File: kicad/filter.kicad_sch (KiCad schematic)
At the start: 31 parts, among them J4 Conn_01x05, U4 NE5532, U5 NE5532, U6 NE5532, U7 NE5532

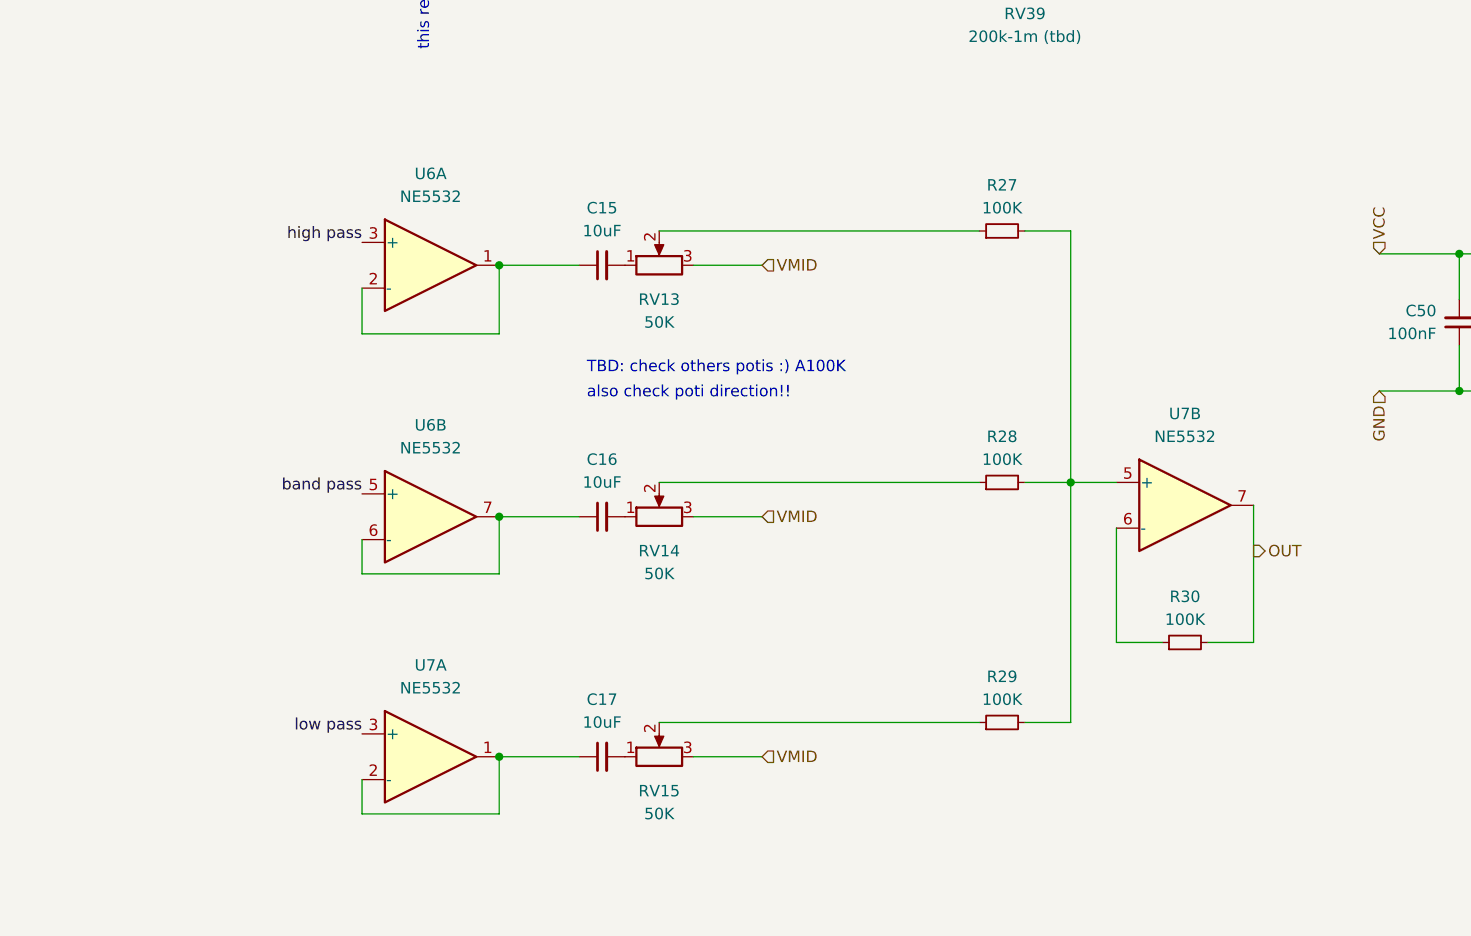
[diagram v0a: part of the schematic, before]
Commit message: fix mixers in filter and compressor, update pcb
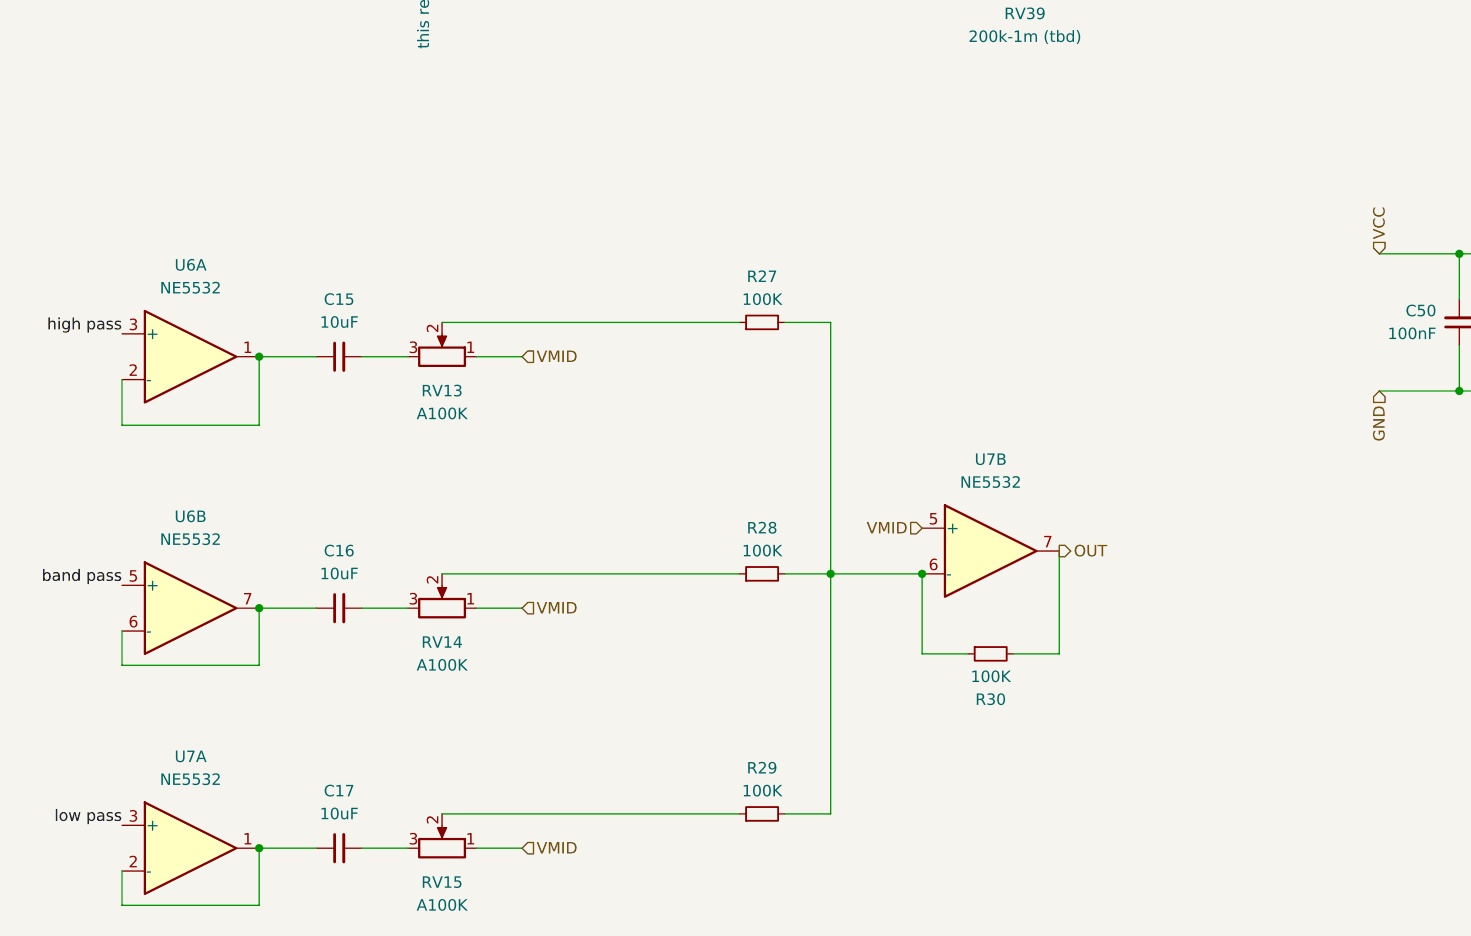
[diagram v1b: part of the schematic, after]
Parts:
- RV13, RV14, RV15: value 50K -> A100K
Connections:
- net VMID: now also RV13.1, RV14.1, RV15.1, U7.5 (+); no longer RV13.3, RV14.3, RV15.3
- net at C16.2: now also RV14.3; no longer RV14.1
- net at C15.2: now also RV13.3; no longer RV13.1
- net at C17.2: now also RV15.3; no longer RV15.1
- net at R27.2, R28.2, R29.2: now also R30.1, U7.6 (-); no longer U7.5 (+)
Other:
- note removed: "TBD: check others potis :) A100K"
- note removed: "also check poti direction!!"
- moved on the sheet: C15, C16, C17, R27, R28, R29, R30, RV13, RV14, RV15, U6A, U6B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

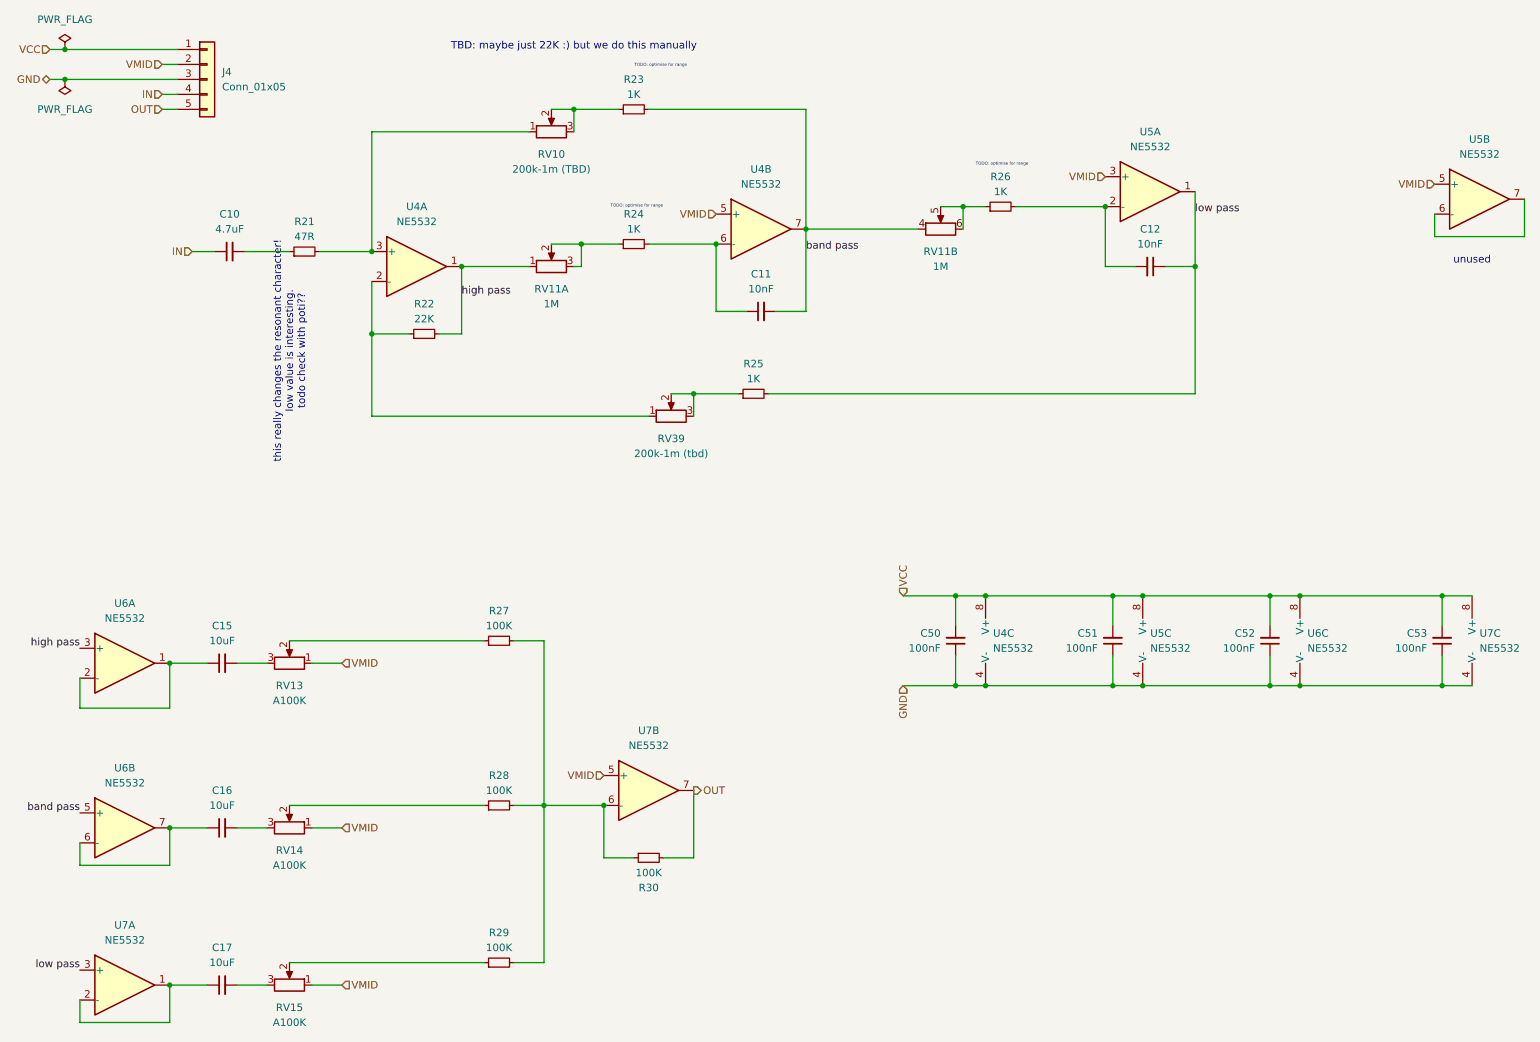
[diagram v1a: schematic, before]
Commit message: mark components as DNP, add LCSC part numbers
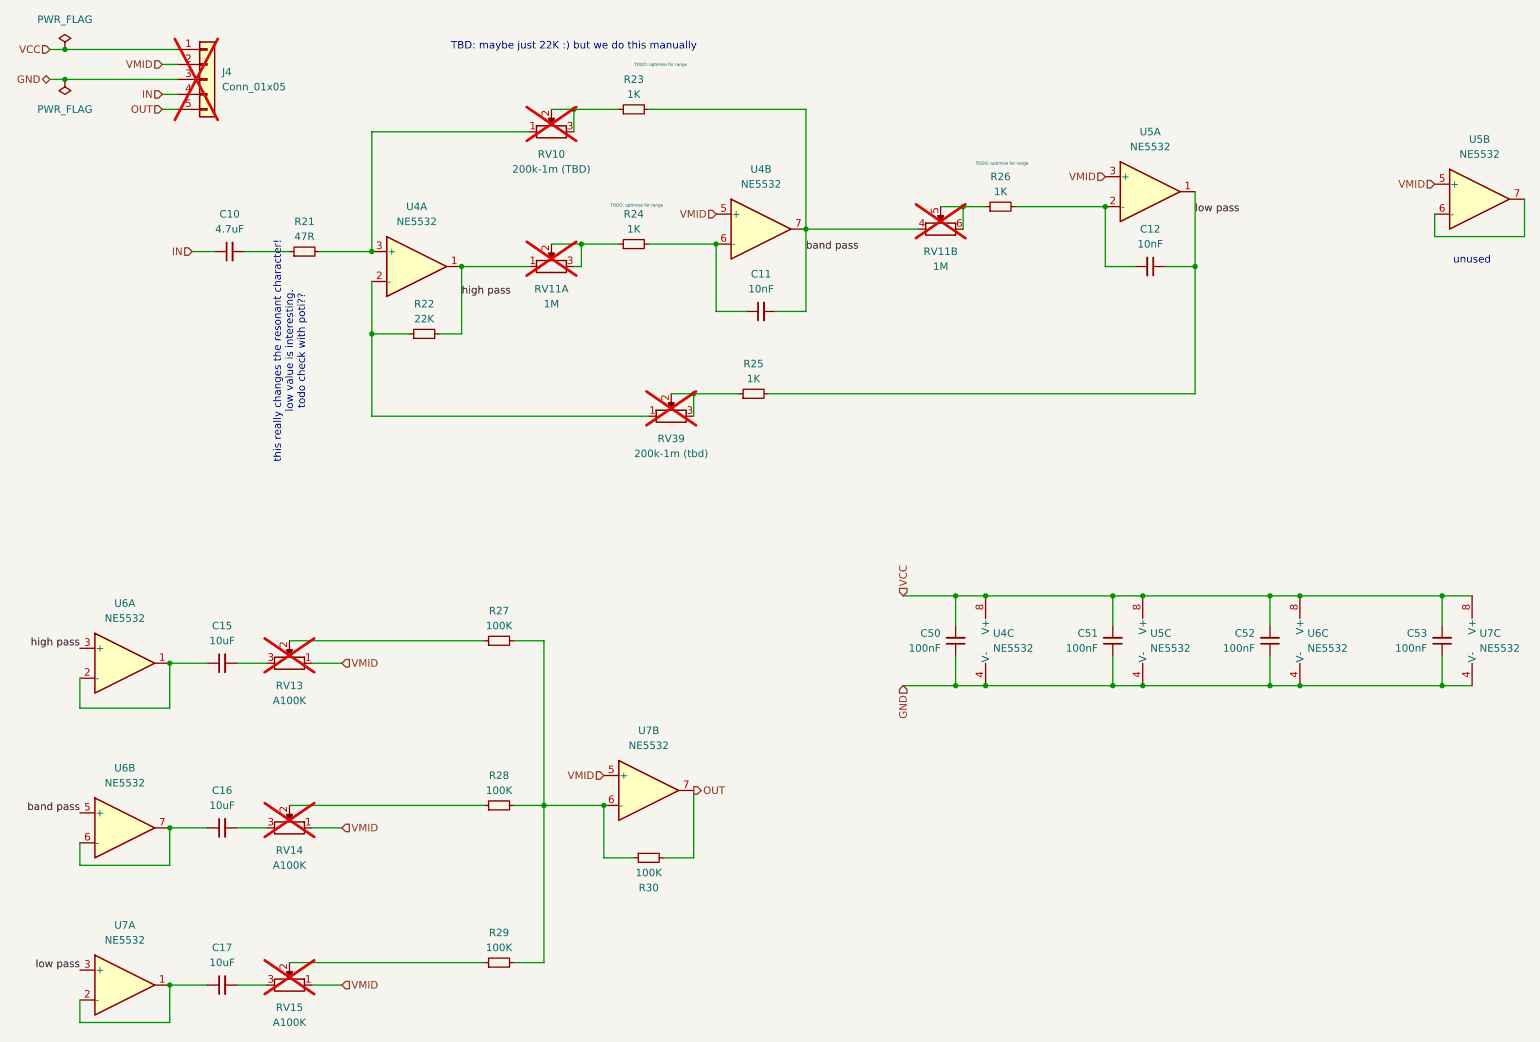
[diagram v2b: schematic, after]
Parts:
- J4, RV10, RV11, RV13, RV14, RV15, RV39: now not fitted
- U4, U5, U6, U7: JLC (none) -> C7426

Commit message: add local changes
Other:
- note added: "low value is interesting here todo check with poti?"
- note added: "tbd: or fixed at 22K"
- note removed: "TBD: maybe just 22K :) but we do this manually"
- note removed: "this really changes the resonant character! low value is interesting. todo check with poti??"
- moved on the sheet: C10, C11, C12, C15, C16, C17, C50, C51, C52, C53, J4, R21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
